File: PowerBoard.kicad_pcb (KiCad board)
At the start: 2 copper layers, 150 x 150 mm, 132 parts, among them IC1 LT1910ES8#PBF, IC2 LT1910ES8#PBF, IC3 LT1910ES8#PBF, IC4 LT1910ES8#PBF, IC5 LT1910ES8#PBF, IC7 MAX17541GATB+T, J1 XT90, J10 XT90, J11 XT90, J12 XT90, J13 XT90, J14 DEAN_T, J15 DEAN_T, J16 DEAN_T, J17 DEAN_T, J18 DEAN_T, J19 DEAN_T, J2 DEAN_T, J20 XT60, J21 XT60, J22 XT60, J23 XT60, J24 XT60, J25 XT60, J26 XT60, J27 XT60, J28 XT60, J29 XT60, J3 XT60, J30 XT60, J31 XT60, J32 XT30, J33 XT30, J34 XT30, J35 XT30, J36 XT30, J37 XT30, J38 XT30, J39 XT30, J4 XT30, J40 XT30, J41 XT60, J5 Conn_01x02, J6 XT90, J7 XT90, J8 XT90, J9 XT90, Q1 IRFS7530TRL7PP, Q2 IRFS7437TRLPBF, Q3 IRFS7437TRLPBF, Q4 IRFS7437TRLPBF, Q5 IRFS7437TRLPBF, U1 Pico, U2 INA238, U3 INA238, U4 INA238, U5 INA238, U6 INA238

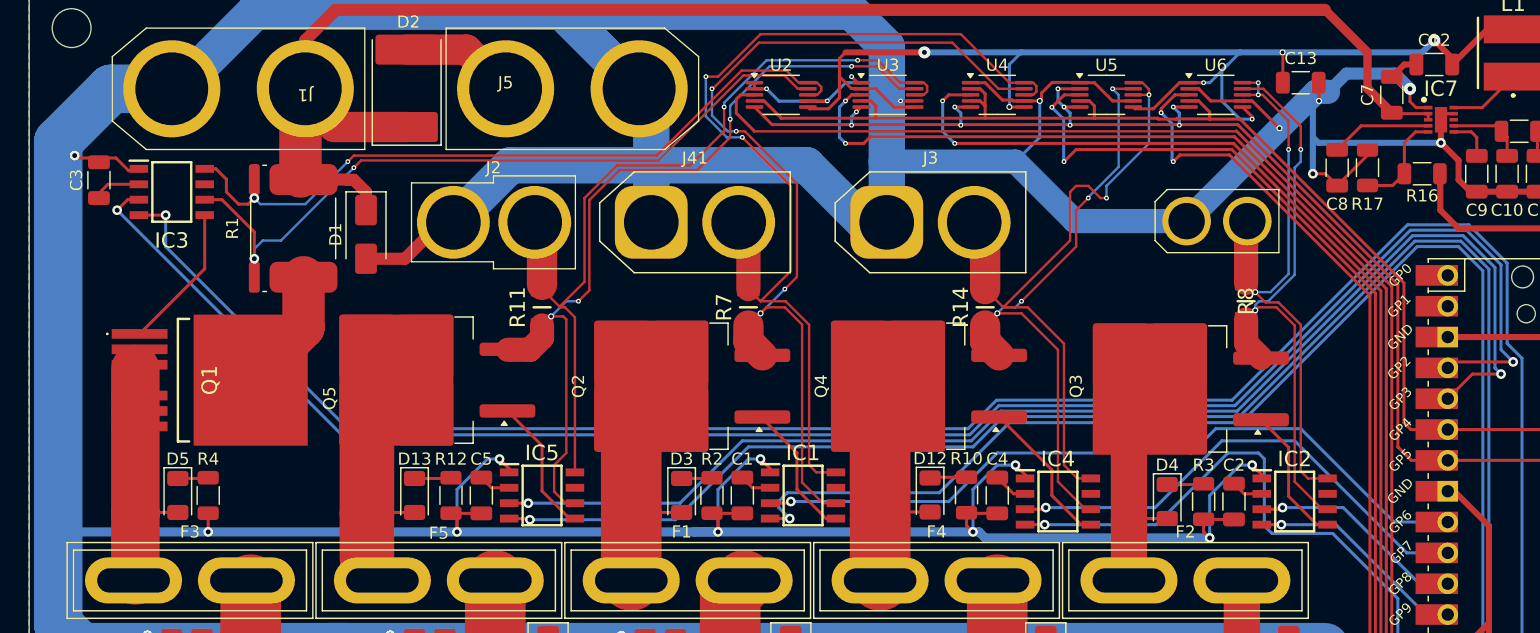
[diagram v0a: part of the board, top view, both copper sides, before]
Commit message: add base resistors for the power mosfets
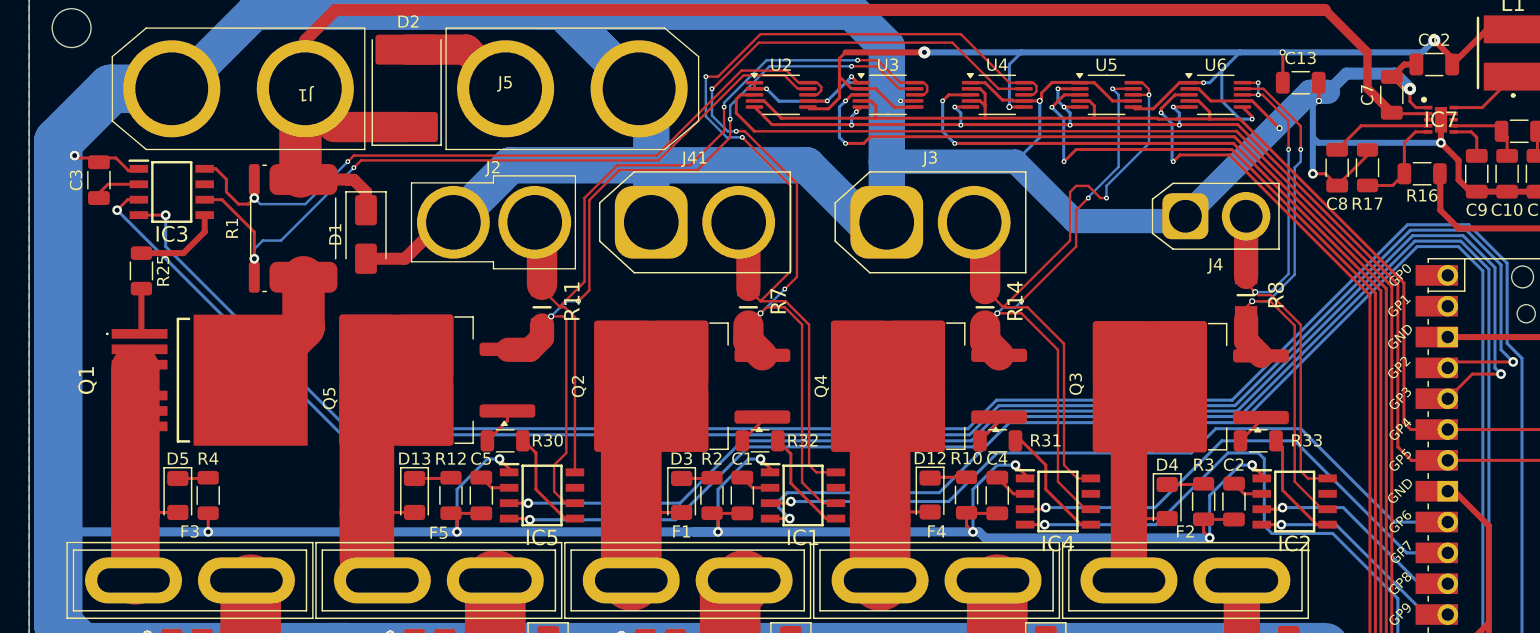
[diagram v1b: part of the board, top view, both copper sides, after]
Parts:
- added R25: 100, Resistor_SMD:R_1206_3216Metric, F.Cu at (34.5, 41.5)
- added R30: 100, Resistor_SMD:R_1206_3216Metric, F.Cu at (64.5, 55.5)
- added R31: 100, Resistor_SMD:R_1206_3216Metric, F.Cu at (105.0, 55.5)
- added R32: 100, Resistor_SMD:R_1206_3216Metric, F.Cu at (85.5, 55.5)
- added R33: 100, Resistor_SMD:R_1206_3216Metric, F.Cu at (126.5, 55.5)
- J4: footprint my_footprint_lib:XT30 -> Connector_AMASS:AMASS_XT30U-F_1x02_P5.0mm_Vertical
- R1: value 4m -> 3m
- moved J4 3.91 mm to (120.5, 37.0)
- moved R8 0.50 mm to (125.5, 43.5)
- moved Q3 0.19 mm to (119.1, 51.0)
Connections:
- J4 pad 1: CURR_5+ -> GND
- J4 pad 2: GND -> CURR_5+
- Q1 pad 1: Net-(IC3-GATE) -> Net-(Q1-G)
- Q2 pad 1: Net-(IC1-GATE) -> Net-(Q2-G)
- Q3 pad 1: Net-(IC2-GATE) -> Net-(Q3-G)
- Q4 pad 1: Net-(IC4-GATE) -> Net-(Q4-G)
- Q5 pad 1: Net-(IC5-GATE) -> Net-(Q5-G)
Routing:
- net Net-(IC3-GATE): track 12.0 -> 7.32 mm
- net Net-(Q1-G): track 0.00 -> 3.79 mm
- net Net-(Q5-G): track 0.00 -> 3.30 mm
- net Net-(IC5-GATE): track 11.4 -> 8.70 mm
- net Net-(Q2-G): track 0.00 -> 2.64 mm
- net Net-(Q3-G): track 0.00 -> 2.62 mm
- net Net-(Q4-G): track 0.00 -> 2.61 mm
- net Net-(IC1-GATE): track 11.3 -> 8.86 mm
- net Net-(IC2-GATE): track 11.4 -> 9.18 mm
- net Net-(IC4-GATE): track 12.5 -> 10.2 mm
- net GND: track 1206.8 -> 1207.5 mm

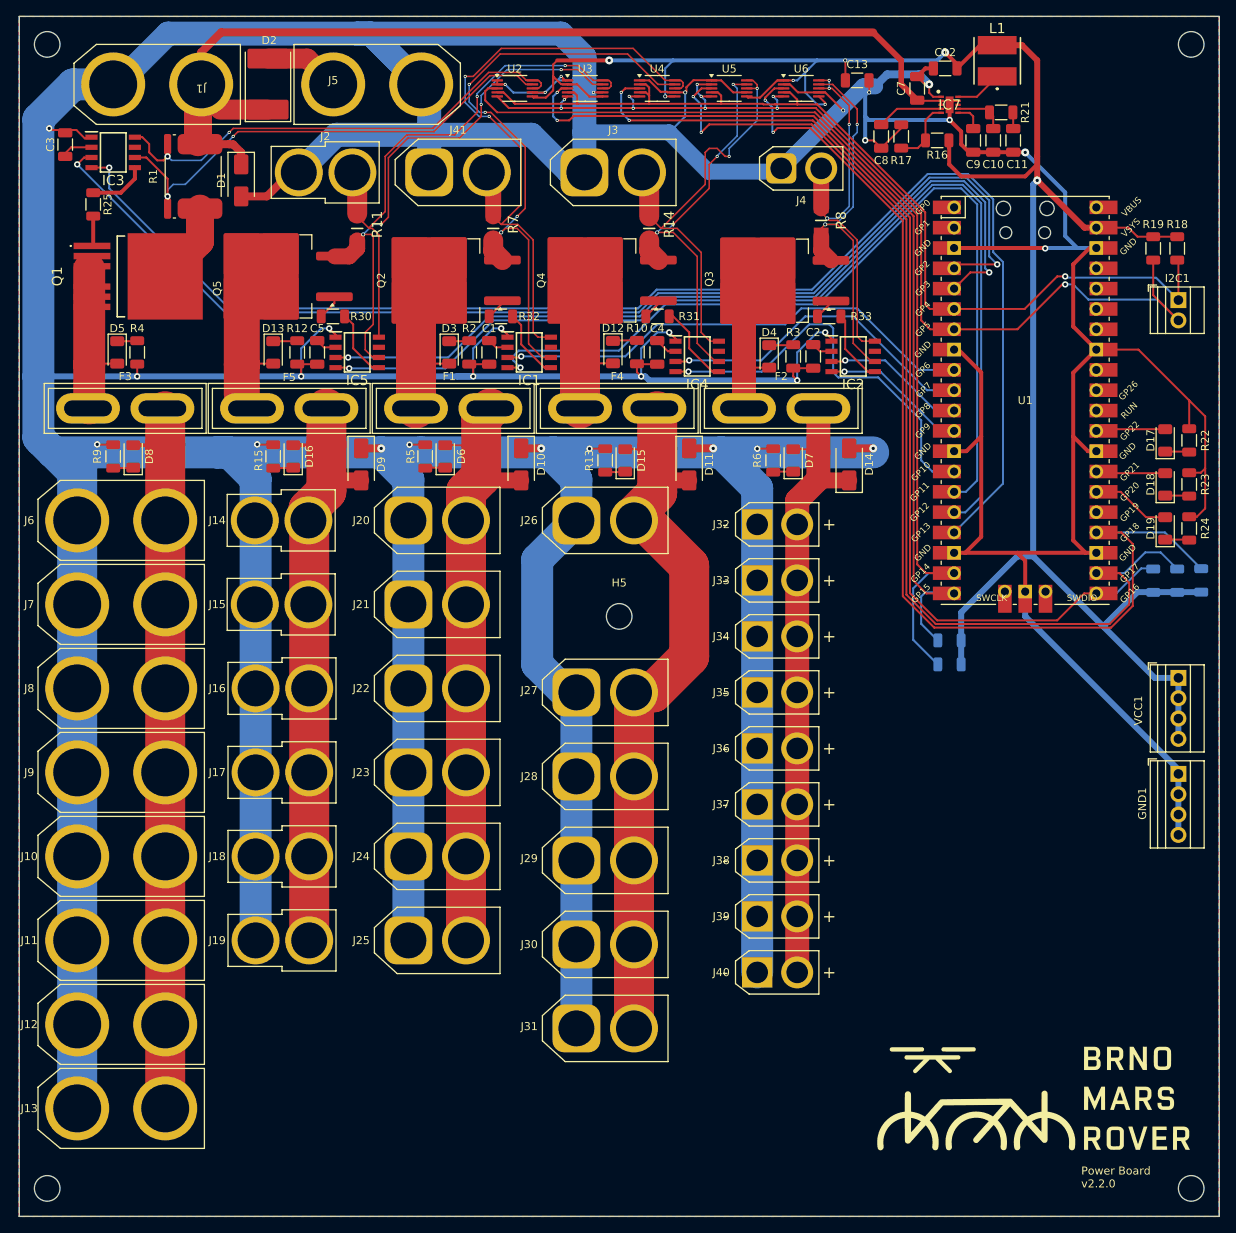
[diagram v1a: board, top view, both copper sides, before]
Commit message: remove solder mask from high current traces and optimize vias for cheaper manufacturing process
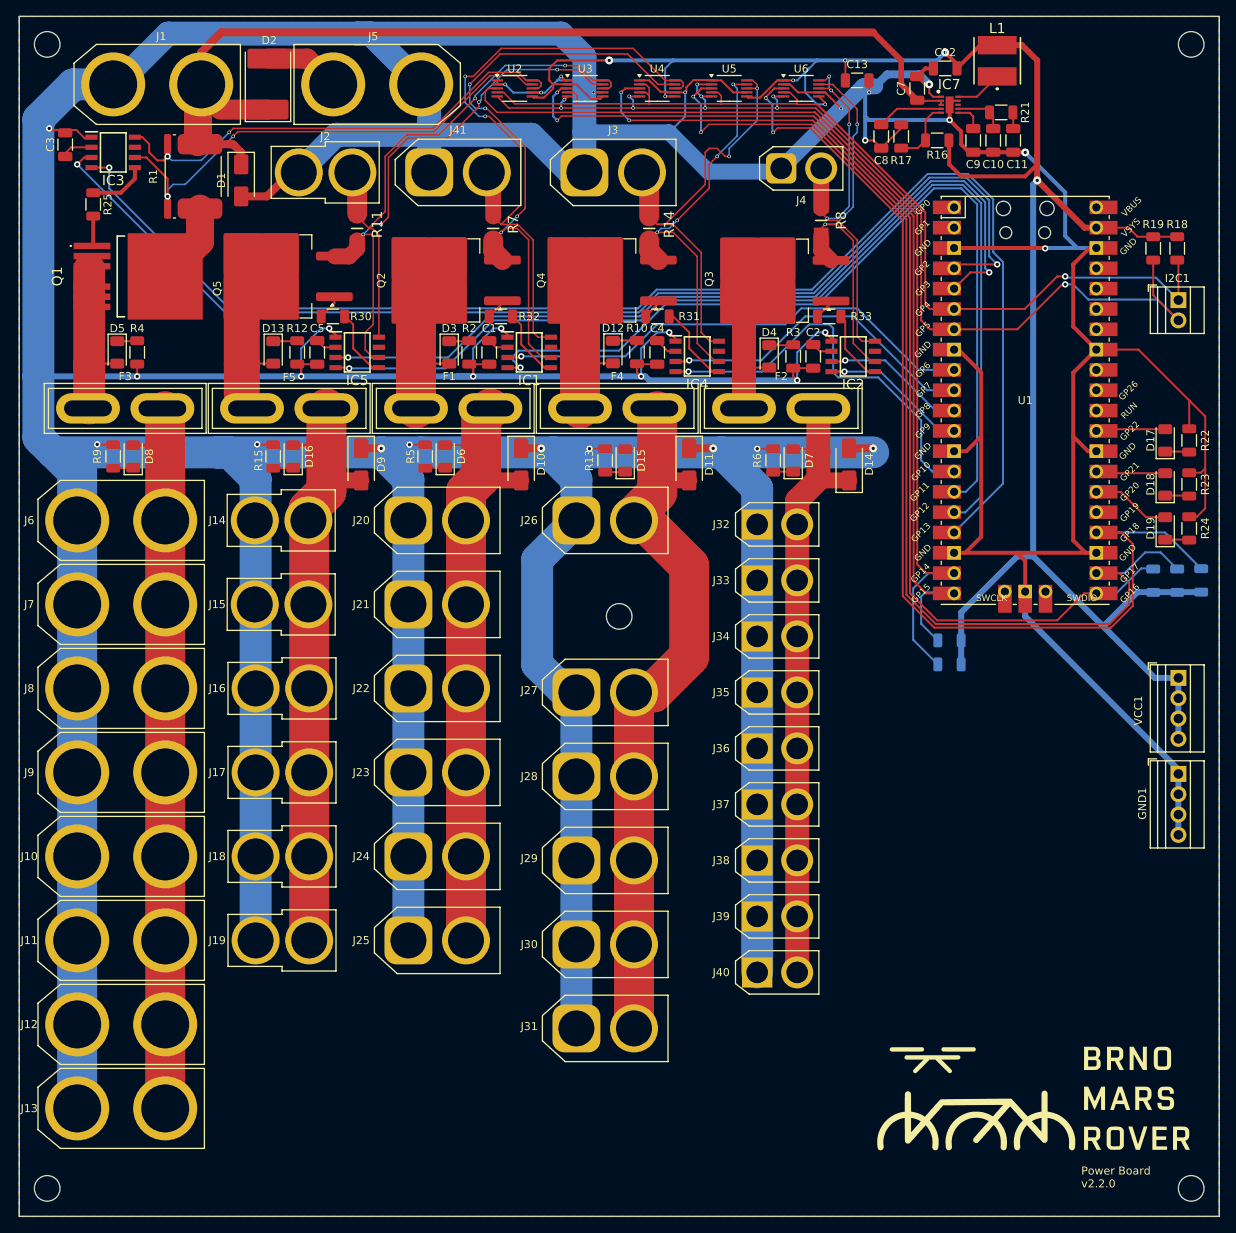
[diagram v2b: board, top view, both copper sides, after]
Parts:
- D1: value SMAJ48A -> SMAJ43A
- D10: value SMAJ30CA -> SMAJ15A
- D11: value SMAJ15CA -> SMAJ12A
- D14: value SMAJ6.5CA -> SMAJ5A
- D9: value SMAJ30CA -> SMAJ24A
- R10, R13, R2, R5: value 6k8 -> 2k2
- R11: value 1m -> 5m
- R12, R15: value 6k8 -> 4k7
- R16: value 80k -> 82k5
- R17: value 17.5k -> 18k2
- R22, R23, R24: value 10k -> 2k2
- R3, R6: value 6k8 -> 470
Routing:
- net CURR_2+: track 69.1 -> 68.0 mm
- net VCC: track 269.2 -> 268.3 mm
- net CURR_2-: track 68.5 -> 67.6 mm
- net CURR_5+: track 48.6 -> 49.4 mm
- net GND: track 1207.5 -> 1206.7 mm

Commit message: safety features added, uart connector added
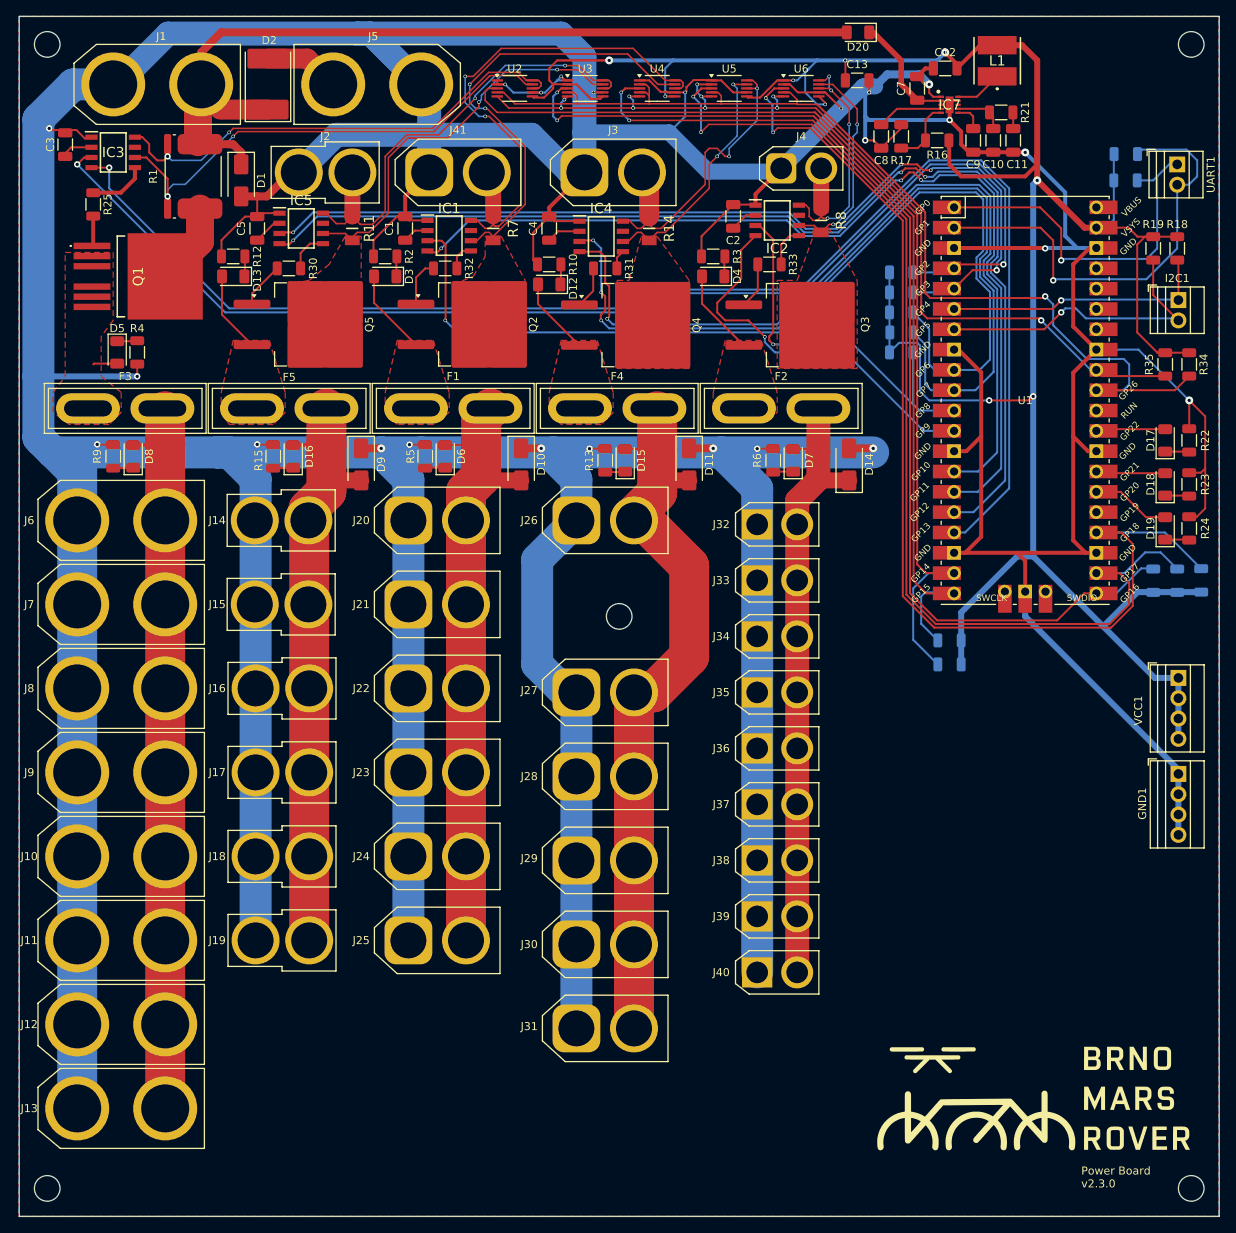
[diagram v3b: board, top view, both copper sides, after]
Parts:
- added D20: D, Diode_SMD:D_1206_3216Metric, F.Cu at (130.1, 20.0)
- added R34: 10k, Resistor_SMD:R_1206_3216Metric, F.Cu at (171.5, 61.5)
- added R35: 10k, Resistor_SMD:R_1206_3216Metric, F.Cu at (168.5, 61.5)
- added R36: 5K, Resistor_SMD:R_1206_3216Metric, B.Cu at (135.5, 50.0)
- added R37: 5K, Resistor_SMD:R_1206_3216Metric, B.Cu at (135.5, 52.5)
- added R38: 5K, Resistor_SMD:R_1206_3216Metric, B.Cu at (135.5, 55.0)
- added R39: 5K, Resistor_SMD:R_1206_3216Metric, B.Cu at (135.5, 57.5)
- added R40: 5K, Resistor_SMD:R_1206_3216Metric, B.Cu at (135.5, 60.0)
- added R41: 10k, Resistor_SMD:R_1206_3216Metric, B.Cu at (163.5, 38.5)
- added R42: 10k, Resistor_SMD:R_1206_3216Metric, B.Cu at (163.6, 35.2)
- added UART1: Screw_Terminal_01x02, TerminalBlock:TerminalBlock_Xinya_XY308-2.54-2P_1x02_P2.54mm_Horizontal, F.Cu at (170.0, 36.5)
- moved C4 20.6 mm to (91.5, 44.5), turned to 90 degrees
- moved C2 20.2 mm to (114.5, 43.0), turned to 90 degrees
- moved IC2 19.5 mm to (120.0, 43.5)
- moved IC4 19.2 mm to (98.0, 45.5)
- moved C1 18.7 mm to (73.5, 44.5), turned to 90 degrees
- moved IC1 17.7 mm to (79.0, 45.4)
- moved C5 17.2 mm to (55.0, 44.5), turned to 90 degrees
- moved IC5 17.0 mm to (60.5, 44.5)
- moved R3 16.0 mm to (112.0, 48.0), turned to 180 degrees
- moved R2 15.9 mm to (71.0, 48.0), turned to 180 degrees
- moved R10 15.5 mm to (91.5, 49.0), turned to 180 degrees
- moved R12 14.4 mm to (52.0, 48.0), turned to 180 degrees
- moved D3 12.4 mm to (71.0, 50.5), turned to 180 degrees
- moved D4 12.2 mm to (112.0, 50.5), turned to 180 degrees
- moved D12 11.6 mm to (91.5, 51.5), turned to 180 degrees
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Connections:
- C7 pad 1: +42V -> Net-(D20-K)
- I2C1 pad 1: SDA -> SDA0
- I2C1 pad 2: SCL -> SCL0
- IC7 pad 2: +42V -> Net-(D20-K)
- IC7 pad 3: +42V -> Net-(D20-K)
- Q2 pad 2: Net-(D3-A) -> CURR_3-
- Q2 pad 3: CURR_3- -> Net-(D3-A)
- Q3 pad 2: Net-(D4-A) -> CURR_5-
- Q3 pad 3: CURR_5- -> Net-(D4-A)
- Q4 pad 2: Net-(D12-A) -> CURR_4-
- Q4 pad 3: CURR_4- -> Net-(D12-A)
- Q5 pad 2: Net-(D13-A) -> CURR_2-
- Q5 pad 3: CURR_2- -> Net-(D13-A)
- R18 pad 2: SDA -> SDA0
- R19 pad 2: SCL -> SCL0
- U1 pad 1: unconnected-(U1-GPIO0-Pad1)_1 -> Net-(U1-GPIO0)
- U1 pad 2: unconnected-(U1-GPIO1-Pad2)_1 -> Net-(U1-GPIO1)
- U1 pad 31: unconnected-(U1-GPIO26_ADC0-Pad31)_1 -> SDA1
- U1 pad 32: unconnected-(U1-GPIO27_ADC1-Pad32)_1 -> SCL1
- U1 pad 6: SDA -> SDA0
- U1 pad 7: SCL -> SCL0
- U2 pad 4: SDA -> SDA1
- U2 pad 5: SCL -> SCL1
- U3 pad 4: SDA -> SDA1
- U3 pad 5: SCL -> SCL1
- U4 pad 2: SDA -> SDA1
- U4 pad 4: SDA -> SDA1
- U4 pad 5: SCL -> SCL1
- U5 pad 2: SCL -> SCL1
- U5 pad 4: SDA -> SDA1
- U5 pad 5: SCL -> SCL1
- U6 pad 4: SDA -> SDA1
- U6 pad 5: SCL -> SCL1
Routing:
- net SCL: track 132.2 -> 0.00 mm, vias 10 -> 0
- net SDA1: track 0.00 -> 132.1 mm, vias 0 -> 1
- net SDA: track 123.2 -> 0.00 mm, vias 1 -> 0
- net SCL1: track 0.00 -> 119.4 mm, vias 0 -> 10
- net GND: track 1206.7 -> 1132.4 mm, vias 31 -> 24
- net FAULT_12V: track 41.0 -> 108.7 mm, vias 1 -> 3
- net VCC: track 268.3 -> 335.1 mm, vias 7 -> 9
- net FAULT_15V: track 61.5 -> 124.3 mm
- net Net-(U1-GPIO1): track 0.00 -> 56.4 mm, vias 0 -> 1
- net EN_12V: track 51.0 -> 107.0 mm
- net Net-(U1-GPIO0): track 0.00 -> 45.9 mm, vias 0 -> 1
- net SCL0: track 0.00 -> 38.6 mm, vias 0 -> 1
- net SDA0: track 0.00 -> 33.6 mm, vias 0 -> 1
- net FAULT_5V: track 18.0 -> 50.1 mm
- net EN_5V: track 18.4 -> 47.7 mm
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- added copper zone on F.Cu, net CURR_2-
- added copper zone on F.Cu, net CURR_3-
- added copper zone on F.Cu, net CURR_4-
- added copper zone on F.Cu, net CURR_5-
- added copper zone on F.Cu, net Net-(D12-A)
- added copper zone on F.Cu, net Net-(D13-A)
- added copper zone on F.Cu, net Net-(D3-A)
- added copper zone on F.Cu, net Net-(D4-A)
- added copper zone on F.Cu, net Net-(D5-A)
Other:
- board text added: "Power Board v2.3.0"
- board text removed: "Power Board v2.2.0"
